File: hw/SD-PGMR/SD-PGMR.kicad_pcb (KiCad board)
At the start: 4 copper layers, 127 x 57.1 mm, 46 parts, among them J1 CONN_01x07 Socket, J2 Conn_01x03 HDR, J3 J-V3.3, J4 Conn_01x03 HDR, Q1 MMBT3906, Q2 MMBT3904, Q3 DMG2305UX, SW1 SW PB-MOM, SW2 SW PB-MOM, U1 74HCT574, U10 SST39SF0n0, U2 74LCX574, U3 AES-Pico, U4 74HCT138, U5 74HCT191, U6 74HCT191, U7 74HCT191, U8 74HCT191, U9 74HCT191

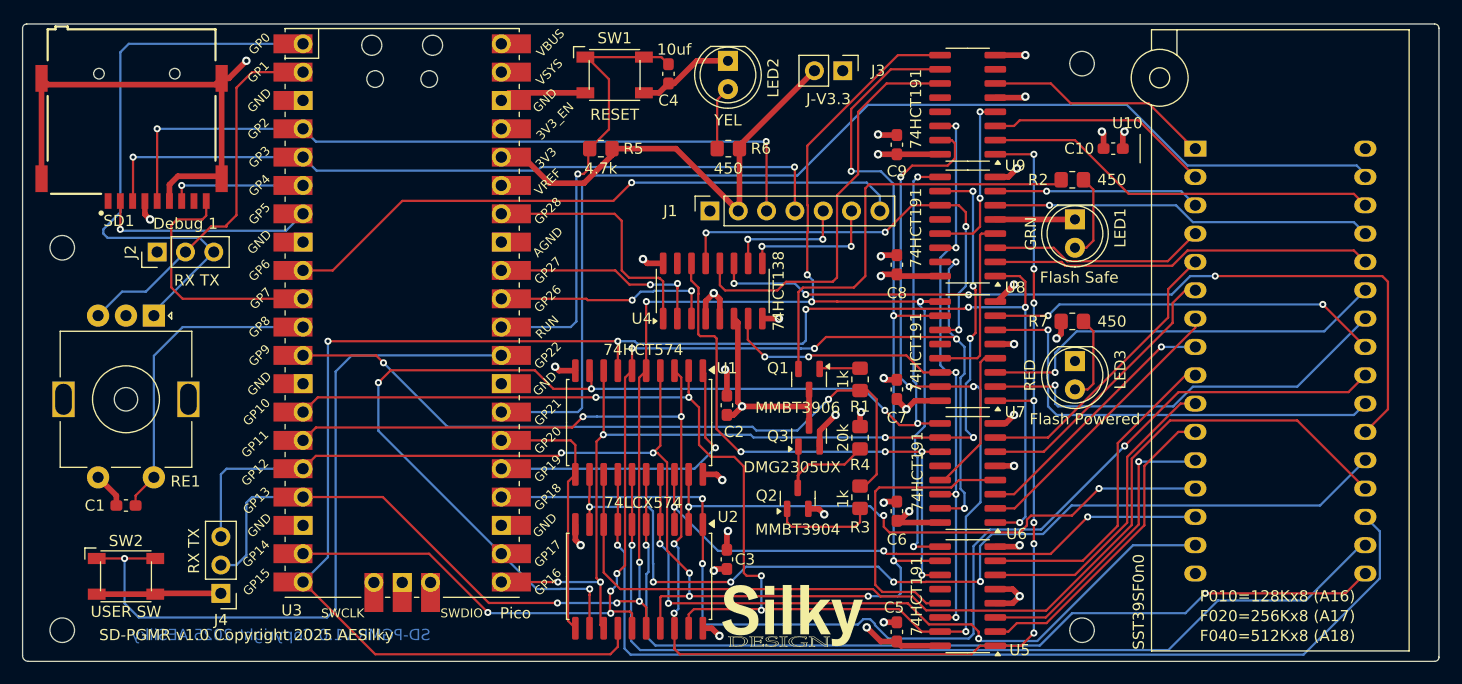
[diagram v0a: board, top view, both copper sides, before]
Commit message: Re-design and re-layout with new power circuit
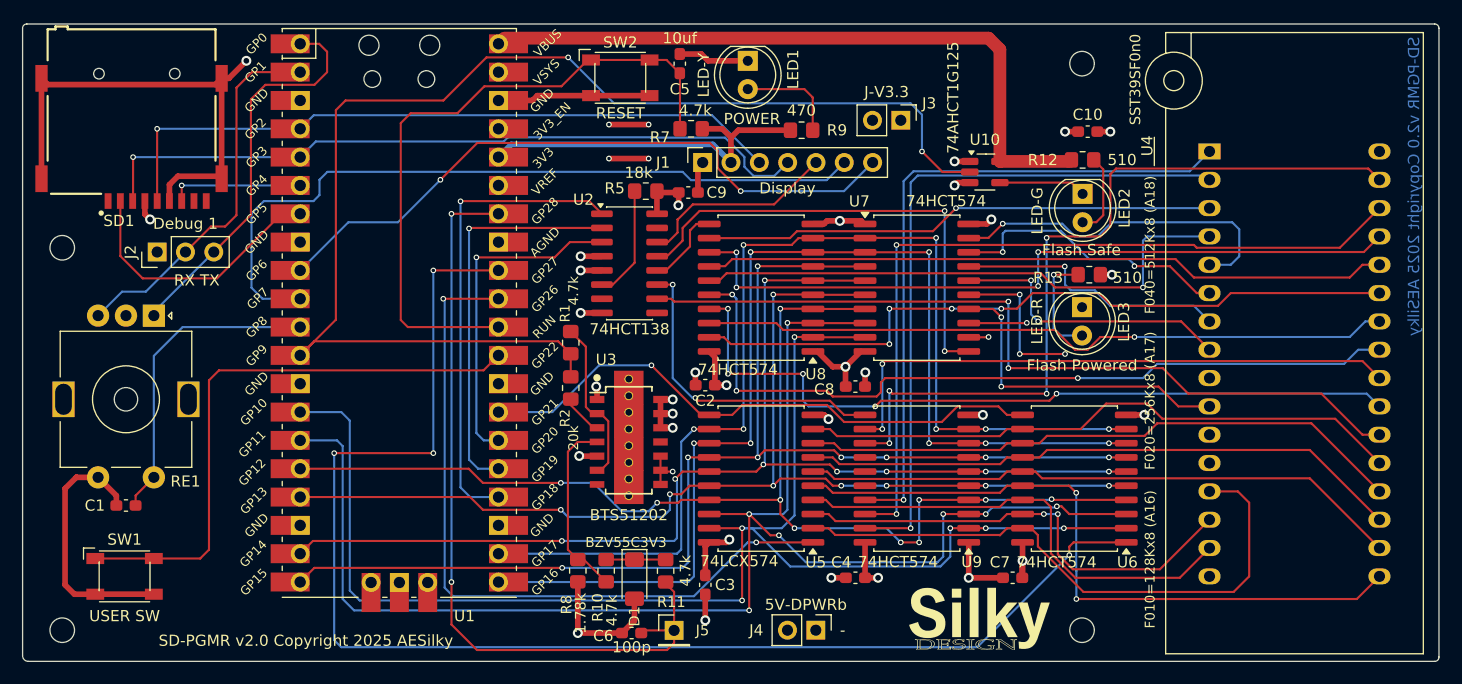
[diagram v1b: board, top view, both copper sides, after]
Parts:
- removed Q1: MMBT3906, Package_TO_SOT_SMD:SOT-23
- removed Q2: MMBT3904, Package_TO_SOT_SMD:SOT-23
- removed Q3: DMG2305UX, Package_TO_SOT_SMD:SOT-23
- removed R3: 1k, Resistor_SMD:R_0805_2012Metric_Pad1.20x1.40mm_HandSolder
- removed R4: 20k, Resistor_SMD:R_0805_2012Metric_Pad1.20x1.40mm_HandSolder
- removed R6: 450, Resistor_SMD:R_0805_2012Metric_Pad1.20x1.40mm_HandSolder
- added D1: BZV55C3V3, Diode_SMD:D_MiniMELF, F.Cu at (131.3, 127.5)
- added J5: HDR 1x1 Pin, Connector_PinHeader_2.54mm:PinHeader_1x01_P2.54mm_Vertical, F.Cu at (134.9, 132.1)
- added R10: 4.7k, Resistor_SMD:R_0805_2012Metric_Pad1.20x1.40mm_HandSolder, F.Cu at (128.8, 126.7)
- added R11: 4.7k, Resistor_SMD:R_0805_2012Metric_Pad1.20x1.40mm_HandSolder, F.Cu at (134.1, 126.8)
- added R12: 510, Resistor_SMD:R_0805_2012Metric_Pad1.20x1.40mm_HandSolder, F.Cu at (171.5, 89.9)
- added R13: 510, Resistor_SMD:R_0805_2012Metric_Pad1.20x1.40mm_HandSolder, F.Cu at (172.1, 100.2)
- added R8: 1.78k, Resistor_SMD:R_0805_2012Metric_Pad1.20x1.40mm_HandSolder, F.Cu at (126.2, 126.7)
- added R9: 470, Resistor_SMD:R_0805_2012Metric_Pad1.20x1.40mm_HandSolder, F.Cu at (146.3, 87.2)
- C4: value 10uf -> 0.1uF
- C5: value 0.1uF -> 10uf
- C6: value 0.1uF -> 100p
- J4: value Conn_01x03 HDR -> CONN 1x2 HDR; footprint Connector_PinHeader_2.54mm:PinHeader_1x03_P2.54mm_Vertical -> Connector_PinHeader_2.54mm:PinHeader_1x02_P2.54mm_Vertical
- LED1: value GRN -> LED-Y
- LED2: value YEL -> LED-G
- LED3: value RED -> LED-R
- R1: value 1k -> 4.7k
- R2: value 450 -> 20k
- R5: value 4.7k -> 18k
- R7: value 450 -> 4.7k
- U1: value 74HCT574 -> AES-Pico; footprint Package_SO:SOIC-20W_7.5x12.8mm_P1.27mm -> AES_Library:AES-RPi_Pico_SMD_TH
- U10: value SST39SF0n0 -> 74AHCT1G125; footprint Socket:DIP_Socket-32_W11.9_W12.7_W15.24_W17.78_W18.5_3M_232-1285-00-0602J -> Package_TO_SOT_SMD:SOT-23-5_HandSoldering
- U2: value 74LCX574 -> 74HCT138; footprint Package_SO:SOIC-20W_7.5x12.8mm_P1.27mm -> Package_SO:SOIC-16_3.9x9.9mm_P1.27mm
- U3: value AES-Pico -> BTS51202; footprint AES_Library:AES-RPi_Pico_SMD_TH -> AES_Library:AES-Inf-BTS5120-DSOP14-BP
- U4: value 74HCT138 -> SST39SF0n0; footprint Package_SO:SOIC-16_3.9x9.9mm_P1.27mm -> Socket:DIP_Socket-32_W11.9_W12.7_W15.24_W17.78_W18.5_3M_232-1285-00-0602J
- U5: value 74HCT191 -> 74LCX574; footprint Package_SO:SOIC-16_3.9x9.9mm_P1.27mm -> Package_SO:SOIC-20W_7.5x12.8mm_P1.27mm
- U6, U7, U8, U9: value 74HCT191 -> 74HCT574; footprint Package_SO:SOIC-16_3.9x9.9mm_P1.27mm -> Package_SO:SOIC-20W_7.5x12.8mm_P1.27mm
- moved SW2 62.9 mm to (130.0, 82.5)
- moved SW1 62.9 mm to (85.6, 127.3)
- moved C5 54.5 mm to (135.4, 81.3), turned to 90 degrees
- moved J4 53.4 mm to (147.6, 132.1), turned to -90 degrees
- moved R2 48.7 mm to (125.6, 110.4), turned to -90 degrees
- moved C4 48.2 mm to (151.1, 127.4), turned to 0 degrees
- moved U4 46.3 mm to (182.9, 89.2), turned to 0 degrees
- moved R7 38.3 mm to (136.4, 87.1), turned to 180 degrees
- moved LED2 34.0 mm to (171.5, 93.0)
- moved U9 33.8 mm to (156.6, 118.5)
- moved LED1 32.6 mm to (141.5, 81.0)
- moved U2 28.1 mm to (130.9, 99.2), turned to 0 degrees
- moved C6 26.2 mm to (131.1, 132.3), turned to 0 degrees
- moved R1 26.2 mm to (125.6, 106.3)
- moved U1 24.8 mm to (110.2, 101.2), turned to 0 degrees
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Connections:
- C10 pad 2: +5VP -> +5DP
- C2 pad 2: +5V -> +5DP
- C4 pad 1: /RESET- -> GND
- C4 pad 2: GND -> +5DP
- C5 pad 1: GND -> /RESET-
- C5 pad 2: +5V -> GND
- C6 pad 2: +5V -> /DPSENS
- C7 pad 2: +5V -> +5DP
- C8 pad 2: +5V -> +5DP
- C9 pad 2: +5V -> +5DP
- J4 pad 2: /PD3 -> Net-(J4-Pin_2)
- LED2 pad 1: GND -> Net-(LED2-K)
- R1 pad 2: Net-(Q1-B) -> Net-(U3-IN0)
- R2 pad 1: Net-(Q1-E) -> /FPWR_ON
- R2 pad 2: Net-(LED1-A) -> Net-(U3-DEN)
- R5 pad 1: +3.3V -> Net-(U2-E3)
- R5 pad 2: /RESET- -> +5DP
- R7 pad 1: +5VP -> +3.3V
- R7 pad 2: Net-(LED3-A) -> /RESET-
- SD1 pad 9: /SD_DET- -> unconnected-(SD1-DET-Pad9)
- SW1 pad 1: /RESET- -> /ATTN-
- SW2 pad 1: Net-(U3-GPIO22) -> /RESET-
- U1 pad 1: /PWR- -> /RE_A
- U1 pad 10: GND -> /DISP_CD
- U1 pad 11: /DATA_LCH -> /RE_SW-
- U1 pad 12: /BD7 -> /FPWR_ON
- U1 pad 13: /BD6 -> GND
- U1 pad 14: /BD5 -> /PD0
- U1 pad 15: /BD4 -> /PD1
- U1 pad 16: /BD3 -> /PD2
- U1 pad 17: /BD2 -> /PD3
- U1 pad 18: /BD1 -> GND
- U1 pad 19: /BD0 -> /PD4
- U1 pad 2: /PD0 -> /RE_B
- U1 pad 20: +5V -> /PD5
- U1 pad 3: /PD1 -> GND
- U1 pad 4: /PD2 -> /SPICK
- U1 pad 5: /PD3 -> /SPIMO
- U1 pad 6: /PD4 -> /SPIMI
- U1 pad 7: /PD5 -> /CARD_CS-
- U1 pad 8: /PD6 -> GND
- U1 pad 9: /PD7 -> /DISP_CS-
- U10 pad 1: /BA18 -> GND
- U10 pad 2: /BA16 -> /FPWR_ON
- U10 pad 3: /BA15 -> GND
- U10 pad 4: /BA12 -> Net-(LED2-K)
- U10 pad 5: /BA7 -> +5V
- U2 pad 1: /PRD- -> /A0
- U2 pad 10: GND -> /F_SEL-
- U2 pad 11: /DATA_LCH -> /ADH_LD-
- U2 pad 12: /PD7 -> /ADM_LD-
- U2 pad 13: /PD6 -> /ADL_LD-
- U2 pad 14: /PD5 -> /DISPRST-
- U2 pad 15: /PD4 -> unconnected-(U2-O0-Pad15)
- U2 pad 16: /PD3 -> +5DP
- U2 pad 2: /BD0 -> /A1
- U2 pad 3: /BD1 -> /A2
- U2 pad 4: /BD2 -> GND
- U2 pad 5: /BD3 -> GND
- U2 pad 6: /BD4 -> Net-(U2-E3)
- U2 pad 7: /BD5 -> unconnected-(U2-O7-Pad7)
- U2 pad 8: /BD6 -> GND
- U2 pad 9: /BD7 -> unconnected-(U2-O6-Pad9)
- U3 pad 1: /RE_A -> GND
- U3 pad 10: /SD_DET- -> Net-(J4-Pin_2)
- U3 pad 11: /RE_SW- -> unconnected-(U3-NC-Pad11)
- U3 pad 12: /FPWR_ON -> +5DP
- U3 pad 13: GND -> +5DP
- U3 pad 14: /PD0 -> +5DP
- U3 pad 2: /RE_B -> Net-(U3-IN0)
- U3 pad 3: GND -> Net-(U3-DEN)
- U3 pad 4: /SPICK -> Net-(U3-IS)
- U3 pad 5: /SPIMO -> GND
- U3 pad 6: /SPIMI -> Net-(U3-IN0)
- U3 pad 7: /CARD_CS- -> unconnected-(U3-NC-Pad7)
- U3 pad 8: GND -> Net-(J4-Pin_2)
- U3 pad 9: /DISP_CS- -> Net-(J4-Pin_2)
- U4 pad 1: /A2 -> /BA18
- U4 pad 10: /DISPRST- -> /BA2
- U4 pad 11: /F_SEL- -> /BA1
- U4 pad 12: /ADH_LD- -> /BA0
- U4 pad 13: /ADM_LD- -> /BD0
- U4 pad 14: /ADL_LD- -> /BD1
- U4 pad 15: unconnected-(U4-O0-Pad15) -> /BD2
- U4 pad 16: +5V -> GND
- U4 pad 2: /A1 -> /BA16
- U4 pad 3: /A0 -> /BA15
- U4 pad 4: GND -> /BA12
- U4 pad 5: GND -> /BA7
- U4 pad 6: +5V -> /BA6
- U4 pad 7: /ACLK -> /BA5
- U4 pad 8: GND -> /BA4
- U4 pad 9: /DISP_CD -> /BA3
- U5 pad 1: /PD1 -> /PRD-
- U5 pad 10: /PD2 -> GND
- U5 pad 11: /ADL_LD- -> /DLATCH
- U5 pad 12: unconnected-(U5-TC-Pad12) -> /PD7
- U5 pad 13: Net-(U5-~{RC}) -> /PD6
- U5 pad 14: /ACLK -> /PD5
- U5 pad 15: /PD0 -> /PD4
- U5 pad 16: +5V -> /PD3
- U5 pad 2: /BA1 -> /BD0
- U5 pad 3: /BA0 -> /BD1
- U5 pad 4: GND -> /BD2
- U5 pad 5: GND -> /BD3
- U5 pad 6: /BA2 -> /BD4
- U5 pad 7: /BA3 -> /BD5
- U5 pad 8: GND -> /BD6
- U5 pad 9: /PD3 -> /BD7
- U6 pad 1: /PD5 -> /PWR-
- U6 pad 10: /PD6 -> GND
- U6 pad 11: /ADL_LD- -> /DLATCH
- U6 pad 12: unconnected-(U6-TC-Pad12) -> /BD7
- U6 pad 13: Net-(U6-~{RC}) -> /BD6
- U6 pad 14: /ACLK -> /BD5
- U6 pad 15: /PD4 -> /BD4
- U6 pad 16: +5V -> /BD3
- U6 pad 2: /BA5 -> /PD0
- U6 pad 3: /BA4 -> /PD1
- U6 pad 4: Net-(U5-~{RC}) -> /PD2
- U6 pad 5: GND -> /PD3
- U6 pad 6: /BA6 -> /PD4
- U6 pad 7: /BA7 -> /PD5
- U6 pad 8: GND -> /PD6
- U7 pad 1: /PD1 -> GND
- U7 pad 10: /PD2 -> GND
- U7 pad 11: /ADM_LD- -> /ADL_LD-
- U7 pad 12: unconnected-(U7-TC-Pad12) -> /BA0
- U7 pad 13: Net-(U7-~{RC}) -> /BA1
- U7 pad 14: /ACLK -> /BA2
- U7 pad 15: /PD0 -> /BA3
- U7 pad 16: +5V -> /BA4
- U7 pad 2: /BA9 -> /PD7
- U7 pad 3: /BA8 -> /PD6
- U7 pad 4: Net-(U6-~{RC}) -> /PD5
- U7 pad 5: GND -> /PD4
- U7 pad 6: /BA10 -> /PD3
- U7 pad 7: /BA11 -> /PD2
- U7 pad 8: GND -> /PD1
- U7 pad 9: /PD3 -> /PD0
- U8 pad 1: /PD5 -> GND
- U8 pad 10: /PD6 -> GND
- U8 pad 12: unconnected-(U8-TC-Pad12) -> /BA15
- U8 pad 13: Net-(U8-~{RC}) -> /BA14
- U8 pad 14: /ACLK -> /BA13
- U8 pad 15: /PD4 -> /BA12
- U8 pad 16: +5V -> /BA11
- U8 pad 2: /BA13 -> /PD0
- U8 pad 3: /BA12 -> /PD1
- U8 pad 4: Net-(U7-~{RC}) -> /PD2
- U8 pad 5: GND -> /PD3
- U8 pad 6: /BA14 -> /PD4
- U8 pad 7: /BA15 -> /PD5
- U8 pad 8: GND -> /PD6
- U9 pad 1: /PD1 -> GND
- U9 pad 10: /PD2 -> GND
- U9 pad 12: unconnected-(U9-TC-Pad12) -> /FRD-
- U9 pad 13: unconnected-(U9-~{RC}-Pad13) -> /FWR-
- U9 pad 14: /ACLK -> unconnected-(U9-Q5-Pad14)
- U9 pad 15: /PD0 -> unconnected-(U9-Q4-Pad15)
- U9 pad 16: +5V -> unconnected-(U9-Q3-Pad16)
- U9 pad 2: /BA17 -> /PD0
- U9 pad 3: /BA16 -> /PD1
- U9 pad 4: Net-(U8-~{RC}) -> /PD2
- U9 pad 5: GND -> /PD3
- U9 pad 6: /BA18 -> /PD4
- U9 pad 7: unconnected-(U9-Q3-Pad7) -> /PD5
- U9 pad 8: GND -> /PD6
- U9 pad 9: /PD3 -> /PD7
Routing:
- net /PWR-: track 27.4 -> 123.5 mm, vias 1 -> 4
- net +5VP: track 75.1 -> 0.00 mm, vias 3 -> 0
- net /ACLK: track 73.5 -> 0.00 mm, vias 7 -> 0
- net /DPSENS: track 0.00 -> 70.6 mm, vias 0 -> 2
- net Net-(U3-GPIO22): track 65.8 -> 0.00 mm, vias 1 -> 0
- net /PD3: track 159.7 -> 102.7 mm, vias 9 -> 8
- net /DISP_CD: track 12.7 -> 67.9 mm, vias 2 -> 0
- net /FRD-: track 0.00 -> 52.7 mm, vias 0 -> 2
- net /ATTN-: track 0.00 -> 52.6 mm
- net /DLATCH: track 0.00 -> 51.7 mm, vias 0 -> 1
- net /FPWR_ON: track 64.2 -> 115.6 mm
- net +5V: track 52.1 -> 101.7 mm, vias 9 -> 0
- net /PD2: track 156.3 -> 107.0 mm, vias 8 -> 10
- net /BA16: track 20.3 -> 61.8 mm, vias 0 -> 1
- net /BA18: track 20.2 -> 60.4 mm, vias 0 -> 1
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- added copper zone on In1.Cu, net +5DP
- removed copper zone on In1.Cu, net +5V
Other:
- board text added: "SD-PGMR v2.0 Copyright 2025 AESilky"
- board text removed: "SD-PGMR v1.0 Copyright 2025 AESilky"
